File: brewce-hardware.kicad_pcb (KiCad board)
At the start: 2 copper layers, 20 parts, among them J1 CONN_01X07, J2 CONN_01X05, P1 CONN_I, P2 CONN_O, Q1 Q_NMOS_DGS, Q2 Q_NMOS_DGS, Q3 Q_NMOS_DGS, U1 MCP1700-3302E_TO92

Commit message: update schematics & PCB
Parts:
- added P3: CONN_DS18B20, Connect:bornier3, F.Cu at (167.6, 108.5)
- added R10: 4.7k, Resistors_ThroughHole:Resistor_Horizontal_RM10mm, F.Cu at (165.4, 124.2)
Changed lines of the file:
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@@
 (kicad_pcb (version 4) (host pcbnew 4.0.2+dfsg1-stable)
   (general
-    (links 44)
-    (no_connects 0)
-    (area 121.71681 99.161 164.261 133.472002)
+    (links 48)
+    (no_connects 4)
+    (area 0 0 0 0)
     (thickness 1.6)
     (drawings 0)
     (tracks 142)
     (zones 0)
-    (modules 20)
-    (nets 19)
+    (modules 22)
+    (nets 20)
   )
   (page A4)
@@
   )
   (setup
-    (last_trace_width 0.5)
+    (last_trace_width 0.25)
     (user_trace_width 0.5)
     (trace_clearance 0.2)
@@
   (net 17 /IO_O)
   (net 18 "Net-(Q3-Pad1)")
+  (net 19 "Net-(P3-Pad2)")
   (net_class Default "This is the default net class."
     (clearance 0.2)
@@
     (add_net /Simblee/GPIO6)
     (add_net GND)
+    (add_net "Net-(P3-Pad2)")
     (add_net "Net-(Q3-Pad1)")
     (add_net VAA)
@@
     )
   )
-  (segment (start 148.082 116.078) (end 148.082 114.808) (width 0.5) (layer B.Cu) (net 1) (status 400000))
-  (segment (start 148.59 114.3) (end 148.59 112.776) (width 0.5) (layer B.Cu) (net 1) (status 800000))
+  (module Resistors_ThroughHole:Resistor_Horizontal_RM10mm (layer F.Cu)
+    (at 165.354 124.206)
+    (descr "Resistor, Axial,  RM 10mm, 1/3W")
+    (tags "Resistor Axial RM 10mm 1/3W")
+    (fp_text reference R10 (at 5.32892 -3.50012) (layer F.SilkS)
+      (effects (font (size 1 1) (thickness 0.15)))
+    )
+    (fp_text value 4.7k (at 5.08 3.81) (layer F.Fab)
+      (effects (font (size 1 1) (thickness 0.15)))
+    )
+    (fp_line (start -1.25 -1.5) (end 11.4 -1.5) (layer F.CrtYd) (width 0.05))
+    (fp_line (start -1.25 1.5) (end -1.25 -1.5) (layer F.CrtYd) (width 0.05))
+    (fp_line (start 11.4 -1.5) (end 11.4 1.5) (layer F.CrtYd) (width 0.05))
+    (fp_line (start -1.25 1.5) (end 11.4 1.5) (layer F.CrtYd) (width 0.05))
+    (fp_line (start 2.54 -1.27) (end 7.62 -1.27) (layer F.SilkS) (width 0.15))
+    (fp_line (start 7.62 -1.27) (end 7.62 1.27) (layer F.SilkS) (width 0.15))
+    (fp_line (start 7.62 1.27) (end 2.54 1.27) (layer F.SilkS) (width 0.15))
+    (fp_line (start 2.54 1.27) (end 2.54 -1.27) (layer F.SilkS) (width 0.15))
+    (fp_line (start 2.54 0) (end 1.27 0) (layer F.SilkS) (width 0.15))
+    (fp_line (start 7.62 0) (end 8.89 0) (layer F.SilkS) (width 0.15))
+    (pad 1 thru_hole circle (at 0 0) (size 1.99898 1.99898) (drill 1.00076) (layers *.Cu *.SilkS *.Mask)
+      (net 19 "Net-(P3-Pad2)"))
+    (pad 2 thru_hole circle (at 10.16 0) (size 1.99898 1.99898) (drill 1.00076) (layers *.Cu *.SilkS *.Mask)
+      (net 1 VDD))
+    (model Resistors_ThroughHole.3dshapes/Resistor_Horizontal_RM10mm.wrl
+      (at (xyz 0 0 0))
+      (scale (xyz 0.4 0.4 0.4))
+      (rotate (xyz 0 0 0))
+    )
+  )
+  (module Connect:bornier3 (layer F.Cu)
+    (at 167.64 108.458 90)
+    (descr "Bornier d'alimentation 3 pins")
+    (tags DEV)
+    (fp_text reference P3 (at 0 -5.08 90) (layer F.SilkS)
+      (effects (font (size 1 1) (thickness 0.15)))
+    )
+    (fp_text value CONN_DS18B20 (at 0 5.08 90) (layer F.Fab)
+      (effects (font (size 1 1) (thickness 0.15)))
+    )
+    (fp_line (start -7.62 3.81) (end -7.62 -3.81) (layer F.SilkS) (width 0.15))
+    (fp_line (start 7.62 3.81) (end 7.62 -3.81) (layer F.SilkS) (width 0.15))
+    (fp_line (start -7.62 2.54) (end 7.62 2.54) (layer F.SilkS) (width 0.15))
+    (fp_line (start -7.62 -3.81) (end 7.62 -3.81) (layer F.SilkS) (width 0.15))
+    (fp_line (start -7.62 3.81) (end 7.62 3.81) (layer F.SilkS) (width 0.15))
+    (pad 1 thru_hole rect (at -5.08 0 90) (size 2.54 2.54) (drill 1.524) (layers *.Cu *.Mask F.SilkS)
+      (net 2 GND))
+    (pad 2 thru_hole circle (at 0 0 90) (size 2.54 2.54) (drill 1.524) (layers *.Cu *.Mask F.SilkS)
+      (net 19 "Net-(P3-Pad2)"))
+    (pad 3 thru_hole circle (at 5.08 0 90) (size 2.54 2.54) (drill 1.524) (layers *.Cu *.Mask F.SilkS)
+      (net 1 VDD))
+    (model Connect.3dshapes/bornier3.wrl
+      (at (xyz 0 0 0))
+      (scale (xyz 1 1 1))
+      (rotate (xyz 0 0 0))
+    )
+  )
+  (segment (start 148.082 116.078) (end 148.082 114.808) (width 0.5) (layer B.Cu) (net 1))
+  (segment (start 148.59 114.3) (end 148.59 112.776) (width 0.5) (layer B.Cu) (net 1))
   (segment (start 148.082 114.808) (end 148.59 114.3) (width 0.5) (layer B.Cu) (net 1))
   (segment (start 142.748 116.078) (end 142.748 117.094) (width 0.5) (layer B.Cu) (net 1))
@@
   (segment (start 134.366 112.522) (end 137.414 112.522) (width 0.5) (layer B.Cu) (net 5))
   (segment (start 137.414 112.522) (end 137.668 112.776) (width 0.5) (layer B.Cu) (net 5))
-  (segment (start 146.812 116.078) (end 146.812 115.062) (width 0.5) (layer B.Cu) (net 6) (status 400000))
+  (segment (start 146.812 116.078) (end 146.812 115.062) (width 0.5) (layer B.Cu) (net 6))
   (via (at 146.05 102.616) (size 1.7) (drill 1) (layers F.Cu B.Cu) (net 6))
   (segment (start 146.05 114.3) (end 146.05 102.616) (width 0.5) (layer F.Cu) (net 6))
@@
   (segment (start 124.968 125.476) (end 128.524 125.476) (width 0.5) (layer B.Cu) (net 16))
   (segment (start 143.256 118.872) (end 143.256 117.856) (width 0.5) (layer B.Cu) (net 17))
-  (segment (start 144.018 117.094) (end 144.018 116.078) (width 0.5) (layer B.Cu) (net 17) (status 800000))
+  (segment (start 144.018 117.094) (end 144.018 116.078) (width 0.5) (layer B.Cu) (net 17))
   (segment (start 143.256 117.856) (end 144.018 117.094) (width 0.5) (layer B.Cu) (net 17))
   (segment (start 143.256 118.872) (end 143.256 131.572) (width 0.5) (layer F.Cu) (net 17))
@@
   (segment (start 143.256 131.572) (end 138.684 131.572) (width 0.5) (layer B.Cu) (net 17))
   (via (at 143.256 131.572) (size 1.7) (drill 1) (layers F.Cu B.Cu) (net 17))
-  (segment (start 149.352 116.078) (end 149.352 123.19) (width 0.5) (layer B.Cu) (net 18) (status 400000))
-  (segment (start 146.812 125.73) (end 144.78 125.73) (width 0.5) (layer B.Cu) (net 18) (status 800000))
+  (segment (start 149.352 116.078) (end 149.352 123.19) (width 0.5) (layer B.Cu) (net 18))
+  (segment (start 146.812 125.73) (end 144.78 125.73) (width 0.5) (layer B.Cu) (net 18))
   (segment (start 149.352 123.19) (end 146.812 125.73) (width 0.5) (layer B.Cu) (net 18))
   (segment (start 141.732 125.73) (end 144.78 125.73) (width 0.5) (layer B.Cu) (net 18))

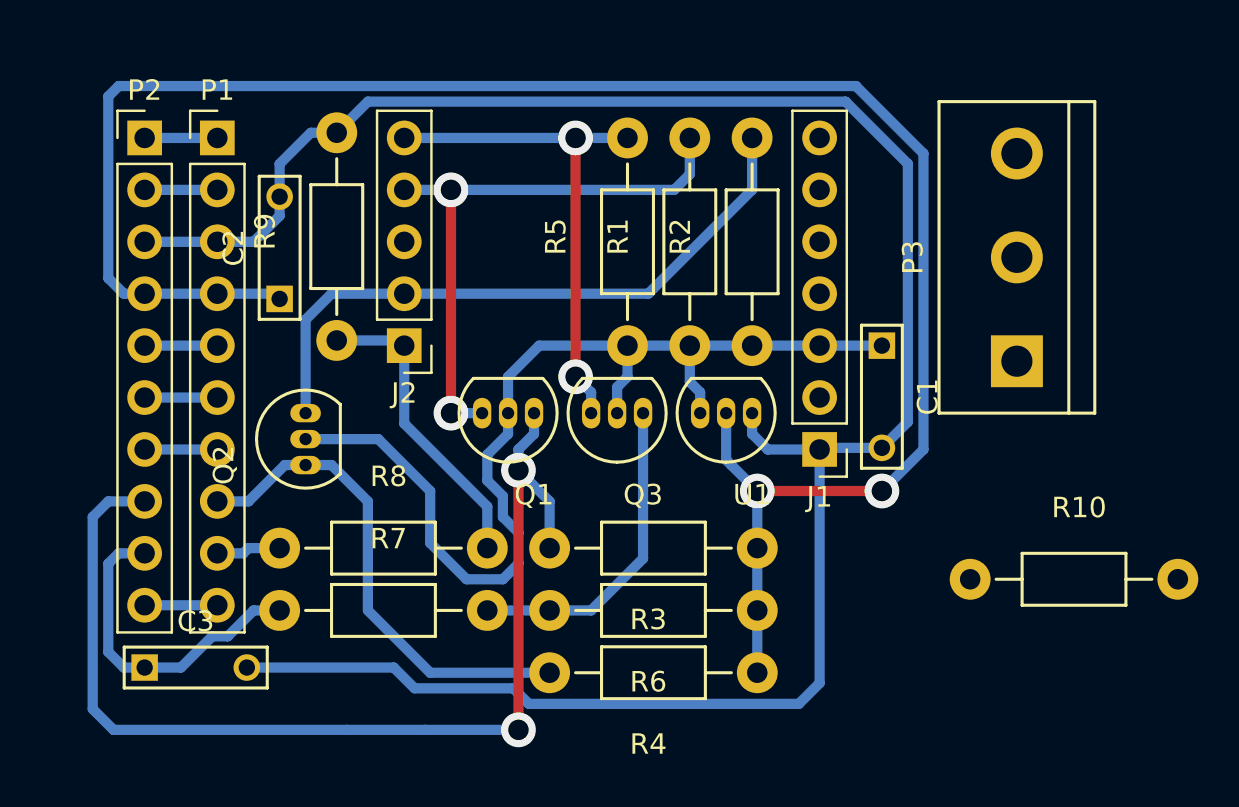
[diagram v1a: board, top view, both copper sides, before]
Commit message: improve schematics, update pcb
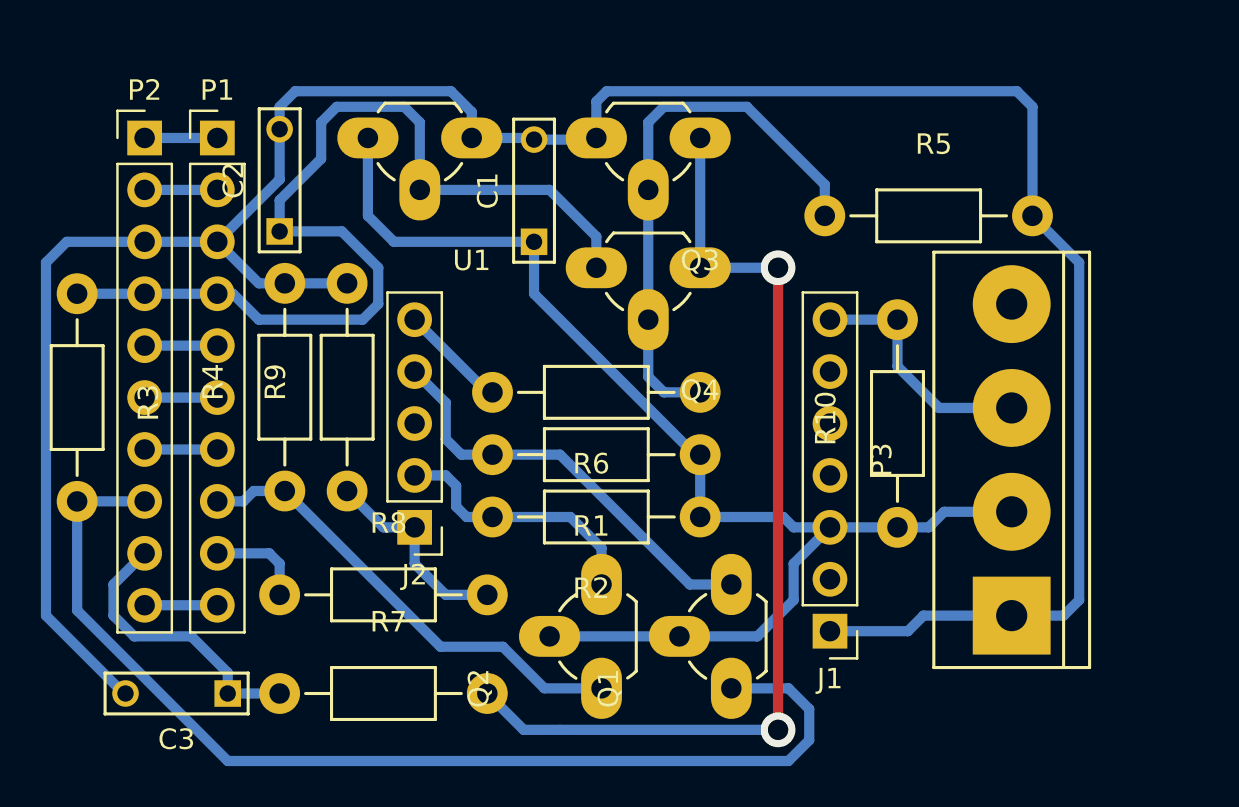
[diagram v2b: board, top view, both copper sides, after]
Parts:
- added Q4: Q_PMOS_DGS, TO_SOT_Packages_THT:TO-92_Rugged, F.Cu at (152.1, 109.0)
- C3: value C -> 1u
- P3: value CONN_DS18B20 -> CONN_01X04; footprint Connect:bornier3 -> Connect:bornier4
- Q1, Q2, Q3: value Q_NMOS_DGS -> 2N7000; footprint TO_SOT_Packages_THT:TO-92_Inline_Narrow_Oval -> TO_SOT_Packages_THT:TO-92_Rugged
- U1: footprint TO_SOT_Packages_THT:TO-92_Inline_Narrow_Oval -> TO_SOT_Packages_THT:TO-92_Rugged
- moved R3 35.5 mm to (121.7, 110.2), turned to 270 degrees
- moved R4 24.8 mm to (131.8, 119.9), turned to 90 degrees
- moved U1 19.2 mm to (141.0, 102.6)
- moved Q2 18.1 mm to (147.3, 129.5)
- moved C1 17.8 mm to (144.0, 107.7), turned to 90 degrees
- moved Q1 16.6 mm to (153.7, 129.5), turned to 90 degrees
- moved Q3 13.7 mm to (152.1, 102.6)
- moved R5 11.6 mm to (158.2, 106.4), turned to 0 degrees
- moved R6 11.0 mm to (152.1, 115.1)
- moved P3 9.91 mm to (167.4, 118.4)
- moved J1 8.90 mm to (158.5, 126.7)
- moved J2 8.90 mm to (138.2, 121.7)
- moved R2 8.76 mm to (152.1, 121.2), turned to 180 degrees
- moved R9 7.38 mm to (134.9, 119.9)
- moved R1 5.36 mm to (152.1, 118.1), turned to 180 degrees
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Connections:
- J1 pad 7: (no net) -> /Simblee/GPIO1
- P3 pad 2: Net-(P3-Pad2) -> VDD
- P3 pad 3: VDD -> /Simblee/GPIO1
- Q3 pad 2: VDD -> Net-(Q3-Pad2)
- Q3 pad 3: /Simblee/GPIO2 -> GND
- R10 pad 1: Net-(P3-Pad2) -> VDD
- R10 pad 2: VDD -> /Simblee/GPIO1
- R4 pad 1: VAA -> /IO_I
- R4 pad 2: /IO_I -> GND
- R5 pad 1: VDD -> Net-(Q3-Pad2)
- R5 pad 2: /Simblee/GPIO2 -> GND
- R6 pad 1: VAA -> Net-(Q3-Pad2)
- R6 pad 2: Net-(Q3-Pad1) -> /Simblee/GPIO2
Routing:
- net VAA: track 95.9 -> 49.0 mm, vias 2 -> 0
- net Net-(Q3-Pad1): track 15.8 -> 47.7 mm, vias 0 -> 2
- net Net-(Q3-Pad2): track 0.00 -> 28.4 mm
- net GND: track 105.7 -> 125.7 mm
- net /Simblee/GPIO2: track 24.7 -> 5.28 mm, vias 2 -> 0
- net /Simblee/GPIO5: track 31.6 -> 13.0 mm
- net /Simblee/GPIO1: track 0.00 -> 12.0 mm
- net VDD: track 51.2 -> 62.2 mm
- net /Simblee/GPIO3: track 28.5 -> 20.8 mm, vias 2 -> 0
- net /Simblee/GPIO6: track 15.0 -> 10.0 mm
- net /Power_O: track 16.2 -> 14.0 mm
- net /Power_I: track 3.15 -> 4.78 mm
- net /IO_I: track 24.3 -> 23.0 mm
- net /IO_O: track 53.8 -> 53.7 mm, vias 2 -> 0

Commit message: fix pwm level shifter
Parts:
- C1, C2: value C -> 1u
- R1, R2, R3, R4, R5: value R -> 10k
- R6: value R -> 100
- R7: value R -> 100k
- moved Q3 5.57 mm to (147.1, 104.9), turned to 0 degrees
- moved Q4 5.38 mm to (147.1, 110.7), turned to 0 degrees
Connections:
- Q3 pad 1: Net-(Q3-Pad1) -> GND
- Q3 pad 3: GND -> Net-(Q3-Pad3)
- Q4 pad 1: Net-(Q3-Pad1) -> VAA
- Q4 pad 3: VAA -> Net-(Q3-Pad3)
- R7 pad 2: Net-(Q3-Pad1) -> Net-(Q3-Pad3)
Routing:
- net Net-(Q3-Pad3): track 0.00 -> 50.4 mm, vias 0 -> 2
- net Net-(Q3-Pad1): track 47.7 -> 0.00 mm, vias 2 -> 0
- net GND: track 125.7 -> 128.5 mm
- net Net-(Q3-Pad2): track 28.4 -> 26.7 mm
- net VDD: track 62.2 -> 63.8 mm
- net VAA: track 49.0 -> 50.4 mm
